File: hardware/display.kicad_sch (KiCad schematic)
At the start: 0 parts

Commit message: Display circuit added
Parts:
- added R10, R11, R12, R13, R14, R15, R16, R17: 330R, symbol Device:R
- added U4: HDSP-7403, Display_7Segment:HDSP-7401, symbol Display_Character:HDSP-7403
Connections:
- new net: R15.2, U4.2 (F)
- new net: R17.2, U4.7 (DP)
- new net: R16.2, U4.3 (G)
- new net: R13.2, U4.5 (D)
- new net: R10.2, U4.10 (A)
- new net: R11.2, U4.9 (B)
- new net: R14.2, U4.4 (E)
- new net: R12.2, U4.8 (C)
- new net DISP_A: R10.1
- new net DISP_B: R11.1
- new net DISP_C: R12.1
- new net DISP_D: R13.1
- new net DISP_E: R14.1
- new net DISP_F: R15.1
- new net DISP_G: R16.1
- new net DISP_P: R17.1
- new net GND: U4.1 (CC), U4.6 (CC)

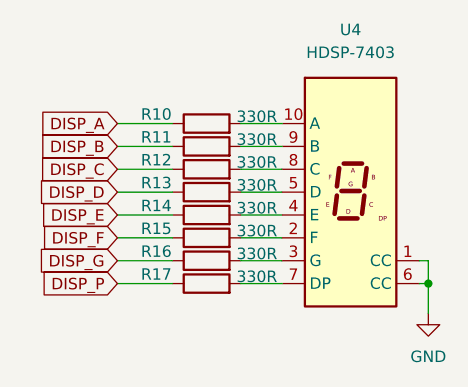
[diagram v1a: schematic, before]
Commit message: Schematics are completed
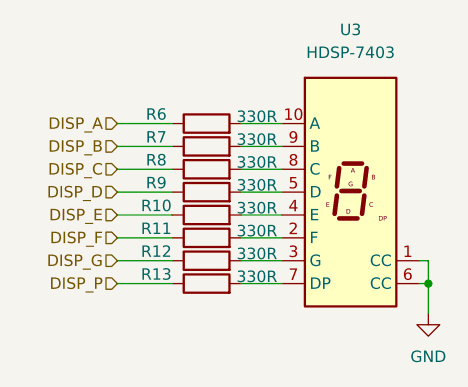
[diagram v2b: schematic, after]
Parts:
- R10: renamed from R14; footprint (none) -> Resistor_SMD:R_0603_1608Metric
- R11: renamed from R15; footprint (none) -> Resistor_SMD:R_0603_1608Metric
- R12: renamed from R16; footprint (none) -> Resistor_SMD:R_0603_1608Metric
- R13: renamed from R17; footprint (none) -> Resistor_SMD:R_0603_1608Metric
- R6: renamed from R10; footprint (none) -> Resistor_SMD:R_0603_1608Metric
- R7: renamed from R11; footprint (none) -> Resistor_SMD:R_0603_1608Metric
- R8: renamed from R12; footprint (none) -> Resistor_SMD:R_0603_1608Metric
- R9: renamed from R13; footprint (none) -> Resistor_SMD:R_0603_1608Metric
- renumbered U4 to U3
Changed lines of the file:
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@@
     (stroke (width 0) (type default) (color 0 0 0 0))
   )
-  (global_label "DISP_E" (shape input) (at 132.588 102.108 180) (fields_autoplaced)
+  (hierarchical_label "DISP_A" (shape input) (at 132.588 91.948 180)
     (effects (font (size 1.27 1.27)) (justify right))
-    (property "Sayfalar Arası Referanslar" "${INTERSHEET_REFS}" (id 0) (at 123.7039 102.0286 0)
-      (effects (font (size 1.27 1.27)) (justify right) hide)
-    )
   )
-  (global_label "DISP_F" (shape input) (at 132.588 104.648 180) (fields_autoplaced)
+  (hierarchical_label "DISP_P" (shape input) (at 132.588 109.728 180)
     (effects (font (size 1.27 1.27)) (justify right))
-    (property "Sayfalar Arası Referanslar" "${INTERSHEET_REFS}" (id 0) (at 123.7644 104.5686 0)
-      (effects (font (size 1.27 1.27)) (justify right) hide)
-    )
   )
-  (global_label "DISP_A" (shape input) (at 132.588 91.948 180) (fields_autoplaced)
+  (hierarchical_label "DISP_E" (shape input) (at 132.588 102.108 180)
     (effects (font (size 1.27 1.27)) (justify right))
-    (property "Sayfalar Arası Referanslar" "${INTERSHEET_REFS}" (id 0) (at 123.7644 91.8686 0)
-      (effects (font (size 1.27 1.27)) (justify right) hide)
-    )
   )
-  (global_label "DISP_C" (shape input) (at 132.588 97.028 180) (fields_autoplaced)
+  (hierarchical_label "DISP_D" (shape input) (at 132.588 99.568 180)
     (effects (font (size 1.27 1.27)) (justify right))
-    (property "Sayfalar Arası Referanslar" "${INTERSHEET_REFS}" (id 0) (at 123.583 96.9486 0)
-      (effects (font (size 1.27 1.27)) (justify right) hide)
-    )
   )
-  (global_label "DISP_D" (shape input) (at 132.588 99.568 180) (fields_autoplaced)
+  (hierarchical_label "DISP_G" (shape input) (at 132.588 107.188 180)
     (effects (font (size 1.27 1.27)) (justify right))
-    (property "Sayfalar Arası Referanslar" "${INTERSHEET_REFS}" (id 0) (at 123.583 99.4886 0)
-      (effects (font (size 1.27 1.27)) (justify right) hide)
-    )
   )
-  (global_label "DISP_G" (shape input) (at 132.588 107.188 180) (fields_autoplaced)
+  (hierarchical_label "DISP_C" (shape input) (at 132.588 97.028 180)
     (effects (font (size 1.27 1.27)) (justify right))
-    (property "Sayfalar Arası Referanslar" "${INTERSHEET_REFS}" (id 0) (at 123.583 107.1086 0)
-      (effects (font (size 1.27 1.27)) (justify right) hide)
-    )
   )
-  (global_label "DISP_B" (shape input) (at 132.588 94.488 180) (fields_autoplaced)
+  (hierarchical_label "DISP_F" (shape input) (at 132.588 104.648 180)
     (effects (font (size 1.27 1.27)) (justify right))
-    (property "Sayfalar Arası Referanslar" "${INTERSHEET_REFS}" (id 0) (at 123.583 94.4086 0)
-      (effects (font (size 1.27 1.27)) (justify right) hide)
-    )
   )
-  (global_label "DISP_P" (shape input) (at 132.588 109.728 180) (fields_autoplaced)
+  (hierarchical_label "DISP_B" (shape input) (at 132.588 94.488 180)
     (effects (font (size 1.27 1.27)) (justify right))
-    (property "Sayfalar Arası Referanslar" "${INTERSHEET_REFS}" (id 0) (at 123.583 109.6486 0)
-      (effects (font (size 1.27 1.27)) (justify right) hide)
-    )
   )
   (symbol (lib_id "Device:R") (at 142.494 104.648 90) (unit 1)
     (in_bom yes) (on_board yes)
-    (property "Reference" "R15" (id 0) (at 136.906 103.632 90))
+    (property "Reference" "R11" (id 0) (at 136.906 103.632 90))
     (property "Value" "330R" (id 1) (at 148.082 103.886 90))
-    (property "Footprint" "" (id 2) (at 142.494 106.426 90)
+    (property "Footprint" "Resistor_SMD:R_0603_1608Metric" (id 2) (at 142.494 106.426 90)
       (effects (font (size 1.27 1.27)) hide)
     )
@@
   (symbol (lib_id "Device:R") (at 142.494 109.728 90) (unit 1)
     (in_bom yes) (on_board yes)
-    (property "Reference" "R17" (id 0) (at 136.906 108.712 90))
+    (property "Reference" "R13" (id 0) (at 136.906 108.712 90))
     (property "Value" "330R" (id 1) (at 148.082 108.966 90))
-    (property "Footprint" "" (id 2) (at 142.494 111.506 90)
+    (property "Footprint" "Resistor_SMD:R_0603_1608Metric" (id 2) (at 142.494 111.506 90)
       (effects (font (size 1.27 1.27)) hide)
     )
@@
   (symbol (lib_id "Device:R") (at 142.494 107.188 90) (unit 1)
     (in_bom yes) (on_board yes)
-    (property "Reference" "R16" (id 0) (at 136.906 106.172 90))
+    (property "Reference" "R12" (id 0) (at 136.906 106.172 90))
     (property "Value" "330R" (id 1) (at 148.082 106.426 90))
-    (property "Footprint" "" (id 2) (at 142.494 108.966 90)
+    (property "Footprint" "Resistor_SMD:R_0603_1608Metric" (id 2) (at 142.494 108.966 90)
       (effects (font (size 1.27 1.27)) hide)
     )
@@
   (symbol (lib_id "Device:R") (at 142.494 99.568 90) (unit 1)
     (in_bom yes) (on_board yes)
-    (property "Reference" "R13" (id 0) (at 136.906 98.552 90))
+    (property "Reference" "R9" (id 0) (at 136.906 98.552 90))
     (property "Value" "330R" (id 1) (at 148.082 98.806 90))
-    (property "Footprint" "" (id 2) (at 142.494 101.346 90)
+    (property "Footprint" "Resistor_SMD:R_0603_1608Metric" (id 2) (at 142.494 101.346 90)
       (effects (font (size 1.27 1.27)) hide)
     )
@@
   (symbol (lib_id "power:GND") (at 167.132 113.03 0) (unit 1)
     (in_bom yes) (on_board yes) (fields_autoplaced)
-    (property "Reference" "#PWR020" (id 0) (at 167.132 119.38 0)
+    (property "Reference" "#PWR019" (id 0) (at 167.132 119.38 0)
       (effects (font (size 1.27 1.27)) hide)
     )
@@
   (symbol (lib_id "Device:R") (at 142.494 91.948 90) (unit 1)
     (in_bom yes) (on_board yes)
-    (property "Reference" "R10" (id 0) (at 136.906 90.932 90))
+    (property "Reference" "R6" (id 0) (at 136.906 90.932 90))
     (property "Value" "330R" (id 1) (at 148.082 91.186 90))
-    (property "Footprint" "" (id 2) (at 142.494 93.726 90)
+    (property "Footprint" "Resistor_SMD:R_0603_1608Metric" (id 2) (at 142.494 93.726 90)
       (effects (font (size 1.27 1.27)) hide)
     )
@@
   (symbol (lib_id "Device:R") (at 142.494 94.488 90) (unit 1)
     (in_bom yes) (on_board yes)
-    (property "Reference" "R11" (id 0) (at 136.906 93.472 90))
+    (property "Reference" "R7" (id 0) (at 136.906 93.472 90))
     (property "Value" "330R" (id 1) (at 148.082 93.726 90))
-    (property "Footprint" "" (id 2) (at 142.494 96.266 90)
+    (property "Footprint" "Resistor_SMD:R_0603_1608Metric" (id 2) (at 142.494 96.266 90)
       (effects (font (size 1.27 1.27)) hide)
     )
@@
   (symbol (lib_id "Display_Character:HDSP-7403") (at 158.496 99.568 0) (unit 1)
     (in_bom yes) (on_board yes) (fields_autoplaced)
-    (property "Reference" "U4" (id 0) (at 158.496 81.534 0))
+    (property "Reference" "U3" (id 0) (at 158.496 81.534 0))
     (property "Value" "HDSP-7403" (id 1) (at 158.496 84.074 0))
     (property "Footprint" "Display_7Segment:HDSP-7401" (id 2) (at 158.496 113.538 0)
@@
   (symbol (lib_id "Device:R") (at 142.494 102.108 90) (unit 1)
     (in_bom yes) (on_board yes)
-    (property "Reference" "R14" (id 0) (at 136.906 101.092 90))
+    (property "Reference" "R10" (id 0) (at 136.906 101.092 90))
     (property "Value" "330R" (id 1) (at 148.082 101.346 90))
-    (property "Footprint" "" (id 2) (at 142.494 103.886 90)
+    (property "Footprint" "Resistor_SMD:R_0603_1608Metric" (id 2) (at 142.494 103.886 90)
       (effects (font (size 1.27 1.27)) hide)
     )
@@
   (symbol (lib_id "Device:R") (at 142.494 97.028 90) (unit 1)
     (in_bom yes) (on_board yes)
-    (property "Reference" "R12" (id 0) (at 136.906 96.012 90))
+    (property "Reference" "R8" (id 0) (at 136.906 96.012 90))
     (property "Value" "330R" (id 1) (at 148.082 96.266 90))
-    (property "Footprint" "" (id 2) (at 142.494 98.806 90)
+    (property "Footprint" "Resistor_SMD:R_0603_1608Metric" (id 2) (at 142.494 98.806 90)
       (effects (font (size 1.27 1.27)) hide)
     )
